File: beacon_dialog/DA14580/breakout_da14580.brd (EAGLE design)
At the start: 40 x 40 mm, 9 parts

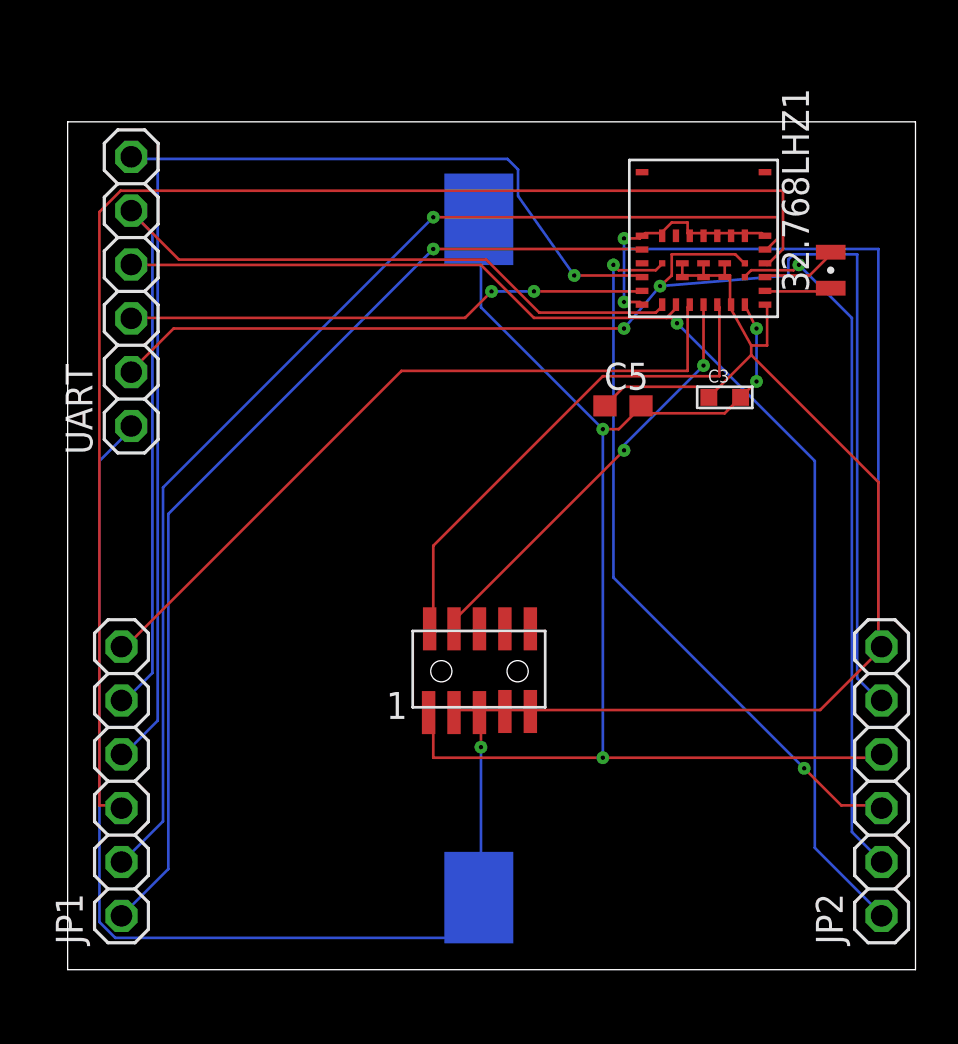
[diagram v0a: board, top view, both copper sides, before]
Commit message: Add new Beacon
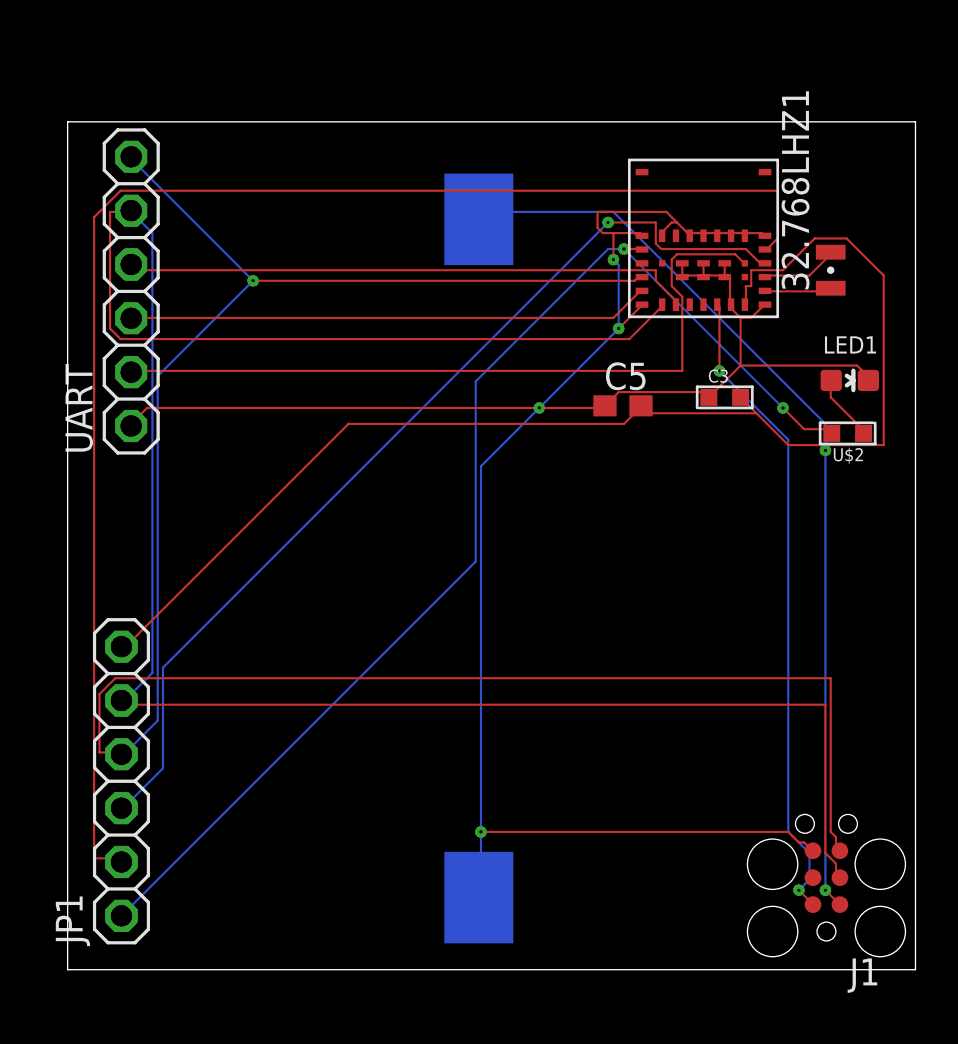
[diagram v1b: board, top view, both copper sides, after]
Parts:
- removed JP2: (no value), adafruit:1X06
- added J1: (no value), tag-connect:TC2030-MCP
- added LED1: (no value), gclue:EIA0603-LED
- U$2: value PIN-HEADER-SMT(1.27MM)2X5 -> RESISTOR0603; device gclue:PIN-HEADER-SMT(1.27MM)2X5 -> GClue-Resistors:0603
- moved U$2 20.7 mm to (36.8, 25.3), turned to 180 degrees
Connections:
- new net N$1: LED1.A, U$2.1
- new net SWDCLK: J1.4
- net +3V3: now also J1.1, JP1.6; no longer JP2.4, U$2.1
- net +5V: no longer JP2.5
- net GND: now also J1.6, LED1.C; no longer JP2.6, U$2.3, U$2.5, U$2.7, U$2.9
- net P0_1: now also U$2.2
- net P0_4: now also J1.5
- net P0_5: now also J1.3
- net P0_6: no longer JP1.6
- net P0_7: no longer JP2.1
- net P1_0: no longer JP2.3
- net P1_1: no longer JP2.2
- net SWCLK: no longer U$2.4
- net SWDIO: now also J1.2; no longer U$2.2
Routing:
- net P0_5: track 51.5 -> 99.5 mm
- net P0_4: track 56.5 -> 98.7 mm
- net GND: track 153.7 -> 111.8 mm, vias 3 -> 4
- net +3V3: track 63.5 -> 104.0 mm, vias 4 -> 2
- net P0_6: track 35.3 -> 0.00 mm
- net P1_0: track 34.4 -> 0.00 mm, vias 2 -> 0
- net P0_7: track 59.7 -> 26.9 mm, vias 1 -> 0
- net P1_1: track 32.6 -> 0.00 mm, vias 1 -> 0
- net +5V: track 64.1 -> 35.4 mm, vias 2 -> 0
- net SWCLK: track 20.4 -> 0.00 mm, vias 2 -> 0
- net P0_3: track 65.7 -> 46.0 mm, vias 0 -> 1
- net P0_2: track 54.6 -> 67.5 mm, vias 1 -> 0
- net P0_1: track 47.4 -> 56.1 mm, vias 1 -> 2
- net SWDIO: track 24.2 -> 30.6 mm, vias 0 -> 2
- net N$1: track 0.00 -> 3.13 mm
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
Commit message: Add update of a14580
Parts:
- moved C3 7.11 mm to (26.5, 21.5)
- moved U$3 3.91 mm to (15.5, 19.6)
- moved JP1 3.73 mm to (3.84, 12.4)
- moved J1 2.94 mm to (34.9, 4.60)
- moved UART 2.06 mm to (3.80, 30.1)
- moved U$1 2.06 mm to (28.1, 33.8)
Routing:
- net GND: track 111.8 -> 153.7 mm, vias 4 -> 3
- net P0_5: track 99.5 -> 83.1 mm
- net +3V3: track 104.0 -> 90.5 mm, vias 2 -> 1
- net P0_4: track 98.7 -> 85.9 mm
- net RST: track 24.6 -> 33.1 mm, vias 0 -> 1
- net +5V: track 35.4 -> 38.5 mm
- net SWDIO: track 30.6 -> 33.6 mm
- net P0_7: track 26.9 -> 24.6 mm, vias 0 -> 2
- net P0_2: track 67.5 -> 65.3 mm, vias 0 -> 1
- net XTAL32KP: track 3.25 -> 5.38 mm
- net XTAL32KM: track 3.64 -> 5.23 mm
- net P0_3: track 46.0 -> 45.3 mm
- net P0_1: track 56.1 -> 55.4 mm
